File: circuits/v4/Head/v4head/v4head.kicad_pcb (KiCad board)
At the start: 2 copper layers, 13 parts, among them J1 Raspberry_Pi_2_3

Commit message: Updates
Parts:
- added 3VMODULE1: Conn_01x03, Connector_JST:JST_EH_B3B-EH-A_1x03_P2.50mm_Vertical, F.Cu at (210.8, 55.9)
- added D1: SK6812MINI, LED_SMD:LED_SK6812MINI_PLCC4_3.5x3.5mm_P1.75mm, F.Cu at (103.3, 79.6)
- added D2: SK6812MINI, LED_SMD:LED_SK6812MINI_PLCC4_3.5x3.5mm_P1.75mm, F.Cu at (121.1, 79.6)
- added D3: SK6812MINI, LED_SMD:LED_SK6812MINI_PLCC4_3.5x3.5mm_P1.75mm, F.Cu at (144.0, 79.6)
- added D4: SK6812MINI, LED_SMD:LED_SK6812MINI_PLCC4_3.5x3.5mm_P1.75mm, F.Cu at (164.3, 79.6)
- added I2CMODULE1: Conn_01x04, Connector_JST:JST_EH_B4B-EH-A_1x04_P2.50mm_Vertical, F.Cu at (195.6, 53.3)
- 5VMODULE1: renamed from SRV2; footprint Connector_Wire:SolderWire-0.1sqmm_1x03_P3.6mm_D0.4mm_OD1mm -> Connector_JST:JST_EH_B3B-EH-A_1x03_P2.50mm_Vertical
- moved 5VMODULE1 102.9 mm to (202.1, 55.9), turned to -90 degrees
- moved RCWL-1 13.0 mm to (95.6, 73.7)
- moved NEO2 2.58 mm to (188.0, 55.9)
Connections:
- J1 pad 18: unconnected-(J1-GPIO24-Pad18) -> Net-(3VMODULE1-Pin_1)
- NEO1 pad 6: Net-(NEO1-NEO_DATA) -> Net-(D1-DIN)
- NEO1 pad 7: Net-(NEO1-NEO_5V) -> Net-(D1-VDD)
- NEO2 pad 1: Net-(NEO1-NEO_DATA) -> Net-(D1-VDD)
- NEO2 pad 2: Net-(NEO1-NEO_5V) -> Net-(D4-DOUT)

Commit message: Updates
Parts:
- removed Serial1: Conn_01x02, Connector_JST:JST_EH_B2B-EH-A_1x02_P2.50mm_Vertical
- added Serial2: Conn_01x02, Connector_JST:JST_XH_B2B-XH-A_1x02_P2.50mm_Vertical, F.Cu at (142.2, 78.7)
- 3VMODULE1, 5VMODULE1, NEO2: footprint Connector_JST:JST_EH_B3B-EH-A_1x03_P2.50mm_Vertical -> Connector_JST:JST_XH_B3B-XH-A_1x03_P2.50mm_Vertical
- I2CMODULE1: footprint Connector_JST:JST_EH_B4B-EH-A_1x04_P2.50mm_Vertical -> Connector_JST:JST_XH_B4B-XH-A_1x04_P2.50mm_Vertical
- J1: footprint Connector_JST:JST_PUD_S40B-PUDSS-1_2x20_P2.00mm_Horizontal -> Connector_PinHeader_2.54mm:PinHeader_2x20_P2.54mm_Vertical
- Power1: footprint Connector_JST:JST_EH_B2B-EH-A_1x02_P2.50mm_Vertical -> Connector_JST:JST_XH_B2B-XH-A_1x02_P2.50mm_Vertical
- SRV1: footprint Connector_Wire:SolderWire-0.1sqmm_1x03_P3.6mm_D0.4mm_OD1mm -> Connector_PinHeader_2.54mm:PinHeader_1x03_P2.54mm_Vertical
- moved 3VMODULE1 27.0 mm to (193.0, 76.2)
- moved AMP1 26.4 mm to (166.5, 48.8)
- moved NEO2 20.9 mm to (182.9, 76.2)
- moved Power1 20.3 mm to (132.1, 78.7)
- moved NEO1 16.5 mm to (162.6, 67.3), turned to 0 degrees
- moved 5VMODULE1 11.9 mm to (193.0, 63.5)
- moved D3 11.7 mm to (155.7, 79.6)
- moved J1 10.3 mm to (182.9, 38.1), turned to -90 degrees
- moved SRV1 7.63 mm to (119.4, 40.6), turned to 90 degrees
- moved I2CMODULE1 5.68 mm to (193.0, 48.3)
- moved MIC1 5.68 mm to (124.5, 50.8)
- moved D4 4.12 mm to (168.4, 79.6)
- moved LLC1 4.02 mm to (135.9, 64.8), turned to 90 degrees
- moved MIC2 2.54 mm to (124.5, 66.0)
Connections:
- 3VMODULE1 pad 2: Net-(3VMODULE1-Pin_2) -> +3V3
- J1 pad 1: Net-(3VMODULE1-Pin_2) -> +3V3
- J1 pad 18: Net-(3VMODULE1-Pin_1) -> unconnected-(J1-GPIO24-Pad18)
- J1 pad 22: Net-(J1-GPIO25) -> Net-(3VMODULE1-Pin_1)
- J1 pad 32: unconnected-(J1-PWM0/GPIO12-Pad32) -> Net-(J1-PWM0/GPIO12)
- LLC1 pad 10: Net-(J1-GPIO25) -> Net-(J1-PWM0/GPIO12)
- LLC1 pad 11: Net-(J1-GPIO15/RXD) -> Net-(J1-GPIO14/TXD)
- LLC1 pad 12: Net-(J1-GPIO14/TXD) -> Net-(J1-GPIO15/RXD)
- LLC1 pad 7: Net-(3VMODULE1-Pin_2) -> +3V3
- LLC1 pad 9: Net-(J1-GPIO26) -> Net-(J1-PWM1/GPIO13)
- MIC1 pad 1: Net-(3VMODULE1-Pin_2) -> +3V3
- MIC1 pad 6: Net-(3VMODULE1-Pin_2) -> +3V3
- MIC2 pad 1: Net-(MIC2-Gnd) -> GND
- MIC2 pad 5: Net-(MIC2-Gnd) -> GND
- MIC2 pad 6: Net-(3VMODULE1-Pin_2) -> +3V3
- NEO1 pad 1: Net-(3VMODULE1-Pin_2) -> +3V3
- RCWL-1 pad 3: Net-(J1-PWM1/GPIO13) -> Net-(J1-GPIO26)

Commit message: Updates to PCB
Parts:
- MIC1, Serial2: moved to B.Cu
- RCWL-1: footprint MakerForgeComponents:RCWL-0516 -> MakerForgeComponents:RCWL-0516_MIN
- moved D1 46.5 mm to (149.7, 83.0), turned to -90 degrees
- moved SRV1 44.9 mm to (141.0, 80.0), turned to 0 degrees
- moved D2 36.9 mm to (157.8, 83.0), turned to -90 degrees
- moved BZ1 26.8 mm to (181.6, 61.0), turned to -90 degrees
- moved RCWL-1 26.2 mm to (117.2, 58.9)
- moved MIC1 26.1 mm to (145.7, 66.0), turned to -90 degrees
- moved 3VMODULE1 23.0 mm to (195.6, 53.4)
- moved MIC2 20.6 mm to (145.1, 66.0), turned to -90 degrees
- moved Serial2 18.2 mm to (124.4, 82.5), turned to 180 degrees
- moved I2CMODULE1 16.7 mm to (195.6, 64.8)
- moved 5VMODULE1 15.5 mm to (195.6, 78.8)
- moved J1 13.0 mm to (185.4, 50.8)
- moved AMP1 11.4 mm to (174.3, 57.1), turned to -90 degrees
- moved D3 10.4 mm to (165.6, 83.0), turned to -90 degrees
- moved NEO1 9.67 mm to (171.4, 71.1)
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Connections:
- D1 pad 2: Net-(D1-VSS) -> GND
- D1 pad 4: Net-(D1-VDD) -> +5V
- D2 pad 2: Net-(D1-VSS) -> GND
- D2 pad 4: Net-(D1-VDD) -> +5V
- D3 pad 2: Net-(D1-VSS) -> GND
- D3 pad 4: Net-(D1-VDD) -> +5V
- D4 pad 2: Net-(D1-VSS) -> GND
- D4 pad 4: Net-(D1-VDD) -> +5V
- NEO1 pad 2: +5V -> GND
- NEO1 pad 3: GND -> Net-(I2CMODULE1-Pin_3)
- NEO1 pad 4: Net-(I2CMODULE1-Pin_3) -> Net-(I2CMODULE1-Pin_2)
- NEO1 pad 5: Net-(I2CMODULE1-Pin_2) -> Net-(D1-DIN)
- NEO2 pad 1: Net-(D1-VDD) -> +5V
- NEO2 pad 3: Net-(D1-VSS) -> GND
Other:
- board outline added: 82.5 x 39.4 mm
- copper layers 2 -> 4

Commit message: Updates to circuit
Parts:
- added D5: SK6812MINI, LED_SMD:LED_SK6812MINI_PLCC4_3.5x3.5mm_P1.75mm, F.Cu at (174.8, 83.0)
- NEO2, Power1: moved to B.Cu
- moved D4 5.16 mm to (168.4, 83.0)
- moved D3 3.54 mm to (162.1, 83.0)
- moved Power1 2.50 mm to (134.6, 82.5), turned to 180 degrees
- moved D2 2.12 mm to (155.7, 83.0)
- moved NEO2 0.92 mm to (184.2, 78.8)
- moved D1 0.76 mm to (149.0, 83.0)
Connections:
- I2CMODULE1 pad 1: +3V3 -> GND
- I2CMODULE1 pad 2: Net-(I2CMODULE1-Pin_2) -> +3V3
- I2CMODULE1 pad 4: GND -> Net-(I2CMODULE1-Pin_4)
- J1 pad 3: Net-(I2CMODULE1-Pin_2) -> Net-(I2CMODULE1-Pin_3)
- J1 pad 5: Net-(I2CMODULE1-Pin_3) -> Net-(I2CMODULE1-Pin_4)
- NEO1 pad 3: Net-(I2CMODULE1-Pin_3) -> Net-(I2CMODULE1-Pin_4)
- NEO1 pad 4: Net-(I2CMODULE1-Pin_2) -> Net-(I2CMODULE1-Pin_3)
- NEO2 pad 1: +5V -> Net-(D5-DOUT)
- NEO2 pad 2: Net-(D4-DOUT) -> +5V
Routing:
- net +3V3: track 0.00 -> 123.0 mm
- net Net-(5VMODULE1-Pin_1): track 0.00 -> 65.1 mm
- net Net-(J1-GPIO14/TXD): track 0.00 -> 63.8 mm
- net Net-(J1-GPIO15/RXD): track 0.00 -> 59.1 mm
- net Net-(I2CMODULE1-Pin_4): track 0.00 -> 51.2 mm
- net Net-(I2CMODULE1-Pin_3): track 0.00 -> 50.5 mm
- net Net-(D1-DIN): track 0.00 -> 40.6 mm
- net Net-(AMP1-BCLK): track 0.00 -> 40.3 mm
- net Net-(3VMODULE1-Pin_1): track 0.00 -> 36.8 mm
- net Net-(AMP1-LRCLK): track 0.00 -> 31.3 mm
- net Net-(J1-PWM0/GPIO12): track 0.00 -> 26.7 mm
- net Net-(J1-GPIO20/MOSI1): track 0.00 -> 24.6 mm
- net Net-(AMP1-DIN): track 0.00 -> 23.5 mm
- net Net-(J1-PWM1/GPIO13): track 0.00 -> 18.9 mm
- net Net-(BZ1--): track 0.00 -> 16.9 mm
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- added copper zone on In1.Cu, net +5V
- added copper zone on In2.Cu, net GND
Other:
- board text added: "+"
- board text added: "-"
- board text added: "3v3"
- board text added: "5v"
- board text added: "TX"
- board text added: "www.makerforge.tech"

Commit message: Updates to circuit
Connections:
- J1 pad 4: unconnected-(J1-5V-Pad4) -> +5V

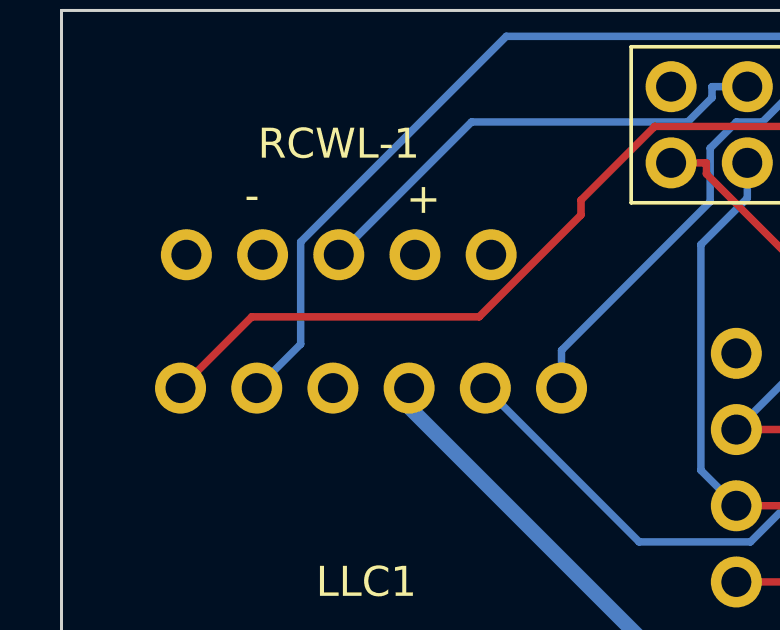
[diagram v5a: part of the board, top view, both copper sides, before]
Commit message: Swap TX & RX to align with LLC
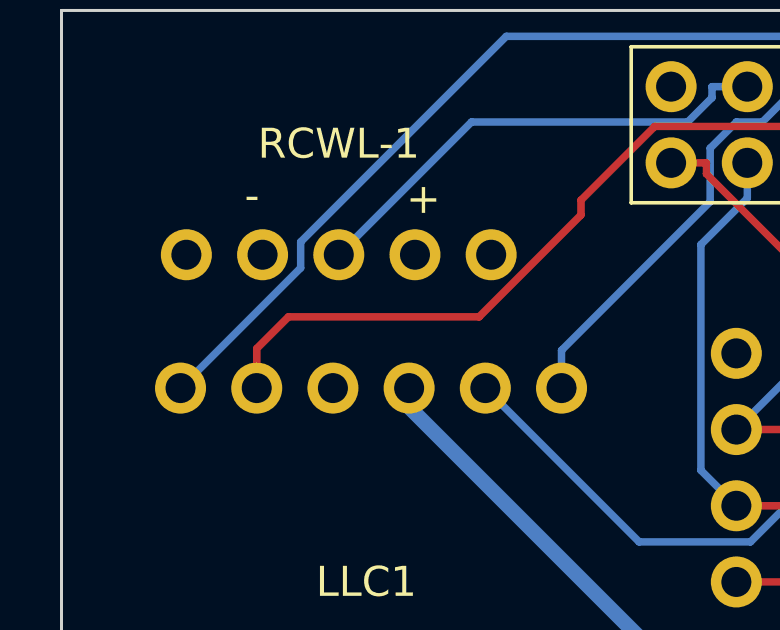
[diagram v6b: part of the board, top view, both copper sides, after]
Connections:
- LLC1 pad 11: Net-(J1-GPIO14/TXD) -> Net-(J1-GPIO15/RXD)
- LLC1 pad 12: Net-(J1-GPIO15/RXD) -> Net-(J1-GPIO14/TXD)
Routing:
- net Net-(J1-GPIO15/RXD): track 59.1 -> 57.3 mm
- net Net-(J1-GPIO14/TXD): track 63.8 -> 64.8 mm
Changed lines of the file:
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@@
       (net 36 "Net-(J1-PWM0{slash}GPIO12)") (pinfunction "LV2") (pintype "power_in"))
     (pad "11" thru_hole circle (at 1.27 11.43 270) (size 1.7 1.7) (drill 1) (layers "*.Cu" "*.Mask")
-      (net 17 "Net-(J1-GPIO14{slash}TXD)") (pinfunction "LV3") (pintype "power_in"))
+      (net 16 "Net-(J1-GPIO15{slash}RXD)") (pinfunction "LV3") (pintype "power_in"))
     (pad "12" thru_hole circle (at 1.27 13.97 270) (size 1.7 1.7) (drill 1) (layers "*.Cu" "*.Mask")
-      (net 16 "Net-(J1-GPIO15{slash}RXD)") (pinfunction "LV4") (pintype "power_in"))
+      (net 17 "Net-(J1-GPIO14{slash}TXD)") (pinfunction "LV4") (pintype "power_in"))
   )
   (footprint "MakerForgeComponents:RCWL-0516_MIN" (layer "F.Cu")
@@
     (effects (font (size 1 1) (thickness 0.15)) (justify mirror))
   )
-  (gr_text "TX" (at 123.825 75.565) (layer "B.SilkS")
+  (gr_text "TX" (at 120.65 75.565) (layer "B.SilkS")
     (effects (font (size 0.8 0.8) (thickness 0.125)) (justify mirror))
   )
@@
   (segment (start 137.43 80.01) (end 130.9675 73.5475) (width 0.25) (layer "B.Cu") (net 15))
   (segment (start 140.97 80.01) (end 137.43 80.01) (width 0.25) (layer "B.Cu") (net 15))
-  (segment (start 130.7609 58.4724) (end 123.1825 58.4724) (width 0.25) (layer "F.Cu") (net 16))
+  (segment (start 123.3475 59.5325) (end 123.3475 60.8475) (width 0.25) (layer "F.Cu") (net 16))
+  (segment (start 130.7609 58.4724) (end 124.4076 58.4724) (width 0.25) (layer "F.Cu") (net 16))
+  (segment (start 175.26 53.34) (end 174.0831 53.34) (width 0.25) (layer "F.Cu") (net 16))
+  (segment (start 174.0831 53.34) (end 174.0831 52.9722) (width 0.25) (layer "F.Cu") (net 16))
   (segment (start 173.2358 52.1249) (end 136.6153 52.1249) (width 0.25) (layer "F.Cu") (net 16))
-  (segment (start 136.6153 52.1249) (end 134.1566 54.5836) (width 0.25) (layer "F.Cu") (net 16))
   (segment (start 134.1566 54.5836) (end 134.1566 55.0767) (width 0.25) (layer "F.Cu") (net 16))
   (segment (start 134.1566 55.0767) (end 130.7609 58.4724) (width 0.25) (layer "F.Cu") (net 16))
-  (segment (start 174.0831 53.34) (end 174.0831 52.9722) (width 0.25) (layer "F.Cu") (net 16))
-  (segment (start 123.1825 58.4725) (end 120.8075 60.8475) (width 0.25) (layer "F.Cu") (net 16))
+  (segment (start 124.4076 58.4724) (end 123.3475 59.5325) (width 0.25) (layer "F.Cu") (net 16))
   (segment (start 174.0831 52.9722) (end 173.2358 52.1249) (width 0.25) (layer "F.Cu") (net 16))
-  (segment (start 123.1825 58.4724) (end 123.1825 58.4725) (width 0.25) (layer "F.Cu") (net 16))
-  (segment (start 175.26 53.34) (end 174.0831 53.34) (width 0.25) (layer "F.Cu") (net 16))
-  (segment (start 124.8125 55.975) (end 124.8125 59.3825) (width 0.25) (layer "B.Cu") (net 17))
+  (segment (start 136.6153 52.1249) (end 134.1566 54.5836) (width 0.25) (layer "F.Cu") (net 16))
+  (segment (start 173.99 51.222) (end 173.99 50.3235) (width 0.25) (layer "B.Cu") (net 17))
+  (segment (start 177.8 53.34) (end 176.6231 53.34) (width 0.25) (layer "B.Cu") (net 17))
+  (segment (start 124.8125 56.8425) (end 120.8075 60.8475) (width 0.25) (layer "B.Cu") (net 17))
+  (segment (start 176.6231 52.9721) (end 175.8141 52.1631) (width 0.25) (layer "B.Cu") (net 17))
   (segment (start 174.9311 52.1631) (end 173.99 51.222) (width 0.25) (layer "B.Cu") (net 17))
+  (segment (start 173.99 50.3235) (end 172.7888 49.1223) (width 0.25) (layer "B.Cu") (net 17))
+  (segment (start 131.6652 49.1223) (end 124.8125 55.975) (width 0.25) (layer "B.Cu") (net 17))
+  (segment (start 124.8125 55.975) (end 124.8125 56.8425) (width 0.25) (layer "B.Cu") (net 17))
+  (segment (start 176.6231 53.34) (end 176.6231 52.9721) (width 0.25) (layer "B.Cu") (net 17))
+  (segment (start 175.8141 52.1631) (end 174.9311 52.1631) (width 0.25) (layer "B.Cu") (net 17))
   (segment (start 172.7888 49.1223) (end 131.6652 49.1223) (width 0.25) (layer "B.Cu") (net 17))
-  (segment (start 176.6231 53.34) (end 176.6231 52.9721) (width 0.25) (layer "B.Cu") (net 17))
-  (segment (start 124.8125 59.3825) (end 123.3475 60.8475) (width 0.25) (layer "B.Cu") (net 17))
-  (segment (start 175.8141 52.1631) (end 174.9311 52.1631) (width 0.25) (layer "B.Cu") (net 17))
-  (segment (start 177.8 53.34) (end 176.6231 53.34) (width 0.25) (layer "B.Cu") (net 17))
-  (segment (start 173.99 51.222) (end 173.99 50.3235) (width 0.25) (layer "B.Cu") (net 17))
-  (segment (start 131.6652 49.1223) (end 124.8125 55.975) (width 0.25) (layer "B.Cu") (net 17))
-  (segment (start 176.6231 52.9721) (end 175.8141 52.1631) (width 0.25) (layer "B.Cu") (net 17))
-  (segment (start 173.99 50.3235) (end 172.7888 49.1223) (width 0.25) (layer "B.Cu") (net 17))
   (segment (start 151.4 64.77) (end 139.335 64.77) (width 0.25) (layer "F.Cu") (net 18))
   (segment (start 139.335 64.77) (end 138.1534 63.5884) (width 0.25) (layer "B.Cu") (net 18))

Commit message: Update annotations
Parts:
- renumbered 3VMODULE1 to 3V_EXT1, 5VMODULE1 to 5V_EXT1, I2CMODULE1 to I2C_EXT1, NEO1 to I2C_NEO1, NEO2 to NEO1, J1 to PI1, Power1 to PWR1, RCWL-1 to RCWL-516, Serial2 to SERIAL1

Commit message: Adjustments
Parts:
- added HOLE: Banana_Jack_1Pin, Connector:Banana_Jack_1Pin, B.Cu at (168.3, 66.0)
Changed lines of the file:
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@@
     (property "Sheetname" "")
     (attr through_hole)
-    (fp_text reference "I2C_NEO1" (at 1.27 4.445 unlocked) (layer "F.SilkS")
+    (fp_text reference "I2C_NEO1" (at 2.54 4.445 unlocked) (layer "F.SilkS")
         (effects (font (size 1 1) (thickness 0.1)))
     )
@@
       (rotate (xyz 0 0 0))
     )
+  )
+  (footprint "Connector:Banana_Jack_1Pin" (layer "B.Cu")
+    (at 168.275 66.04 180)
+    (descr "Single banana socket, footprint - 6mm drill")
+    (tags "banana socket")
+    (attr through_hole)
+    (fp_text reference "HOLE" (at 0 6.5) (layer "B.SilkS")
+        (effects (font (size 1 1) (thickness 0.15)) (justify mirror))
+    )
+    (fp_text value "Banana_Jack_1Pin" (at -0.25 -6.5) (layer "B.Fab")
+        (effects (font (size 1 1) (thickness 0.15)) (justify mirror))
+    )
+    (fp_text user "${REFERENCE}" (at 0 0) (layer "B.Fab")
+        (effects (font (size 0.8 0.8) (thickness 0.12)) (justify mirror))
+    )
+    (fp_circle (center 0 0) (end 5.5 0)
+      (stroke (width 0.12) (type solid)) (fill none) (layer "B.SilkS"))
+    (fp_circle (center 0 0) (end 5.75 0)
+      (stroke (width 0.05) (type solid)) (fill none) (layer "B.CrtYd"))
+    (fp_circle (center 0 0) (end 2 0)
+      (stroke (width 0.1) (type solid)) (fill none) (layer "B.Fab"))
+    (fp_circle (center 0 0) (end 4.85 -0.05)
+      (stroke (width 0.1) (type solid)) (fill none) (layer "B.Fab"))
+    (pad "1" thru_hole circle (at 0 0 180) (size 10.16 10.16) (drill 6.1) (layers "*.Cu" "*.Mask"))
+    (model "${KICAD6_3DMODEL_DIR}/Connector.3dshapes/Banana_Jack_1Pin.wrl"
+      (offset (xyz 0 0 0))
+      (scale (xyz 2 2 2))
+      (rotate (xyz 0 0 0))
+    )
